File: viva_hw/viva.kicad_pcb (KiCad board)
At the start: 2 copper layers, 6 parts, among them Q1 2N3904, Q2 2N3904, Q3 2N3904, Q4 2N3904, U1 XIAO ESP32C3

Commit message: feat: updated footprints
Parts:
- removed U1: XIAO ESP32C3, RF_Module:MCU_Seeed_ESP32C3
- added J1: Conn_01x05_Socket, Connector_PinHeader_2.54mm:PinHeader_1x05_P2.54mm_Vertical, F.Cu at (164.7, 110.1)
- added M1: XIAO_ESP32C3, System_On_Chip:XIAO_ESP32C3_THR, F.Cu at (150.9, 120.4)
- moved ST7735 35.7 mm to (170.0, 111.0)

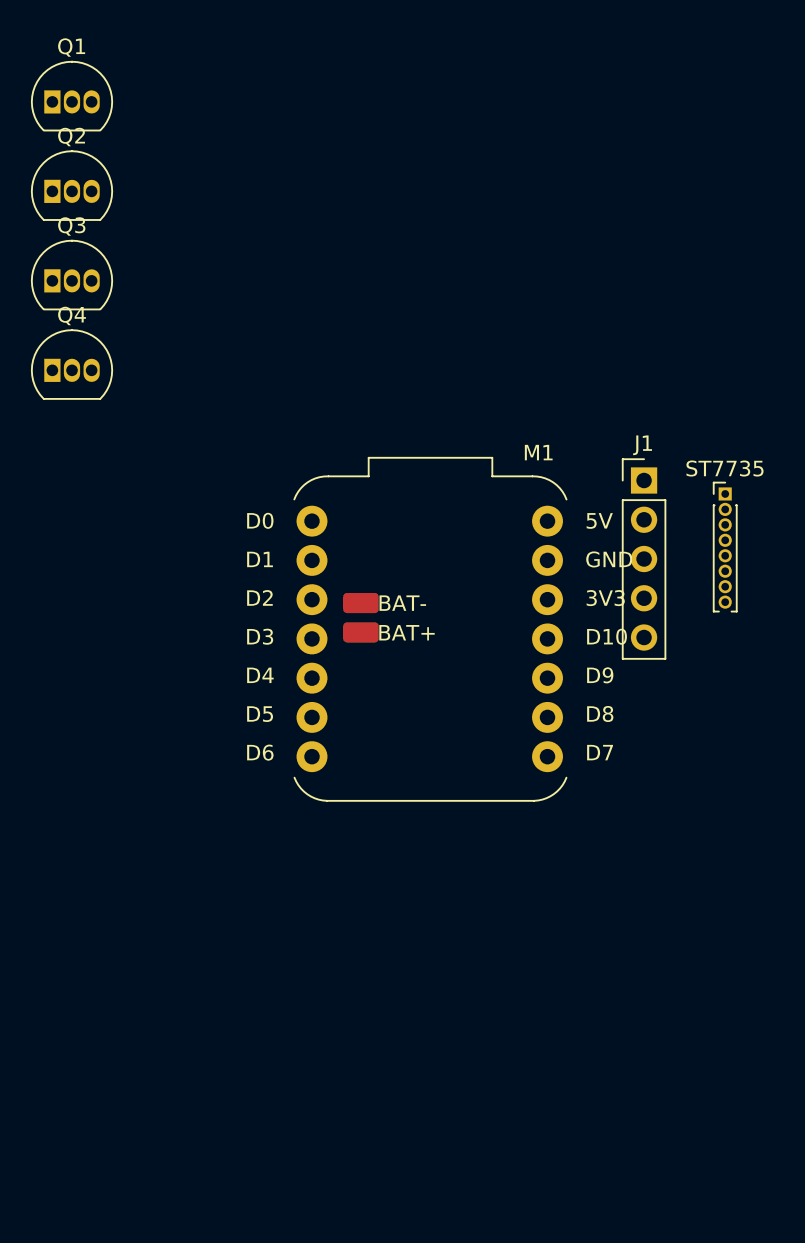
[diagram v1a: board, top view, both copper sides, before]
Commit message: feat: changed socket size for display
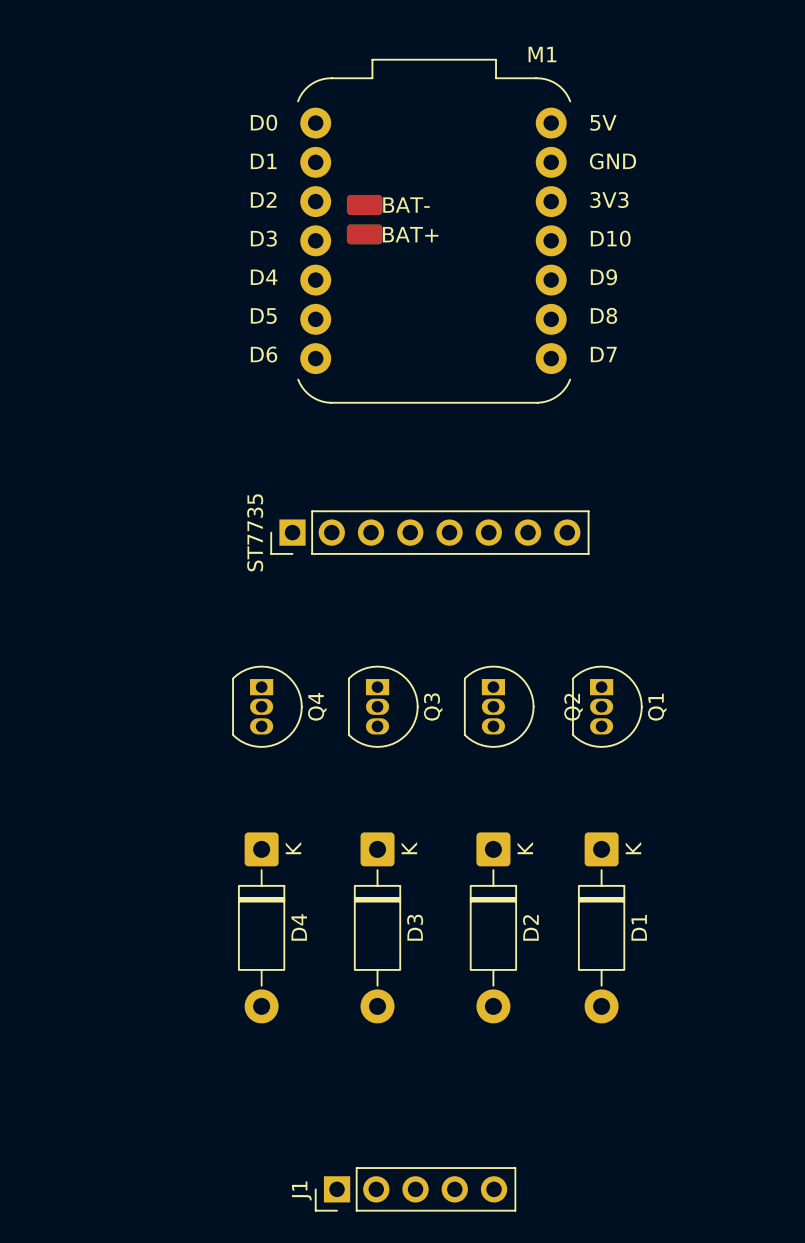
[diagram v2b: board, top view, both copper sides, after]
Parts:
- added D1: 1N4007, Diode_THT:D_DO-41_SOD81_P10.16mm_Horizontal, F.Cu at (162.0, 134.0)
- added D2: 1N4007, Diode_THT:D_DO-41_SOD81_P10.16mm_Horizontal, F.Cu at (155.0, 134.0)
- added D3: 1N4007, Diode_THT:D_DO-41_SOD81_P10.16mm_Horizontal, F.Cu at (147.5, 134.0)
- added D4: 1N4007, Diode_THT:D_DO-41_SOD81_P10.16mm_Horizontal, F.Cu at (140.0, 134.0)
- ST7735: footprint Connector_PinHeader_1.00mm:PinHeader_1x08_P1.00mm_Vertical -> Connector_PinHeader_2.54mm:PinHeader_1x08_P2.54mm_Vertical
- moved Q1 51.9 mm to (162.0, 123.5), turned to -90 degrees
- moved J1 50.0 mm to (144.9, 156.0), turned to 90 degrees
- moved Q2 42.9 mm to (155.0, 123.5), turned to -90 degrees
- moved Q3 33.7 mm to (147.5, 123.5), turned to -90 degrees
- moved ST7735 28.1 mm to (142.0, 113.5), turned to 90 degrees
- moved M1 25.8 mm to (151.2, 94.6)
- moved Q4 24.6 mm to (140.0, 123.5), turned to -90 degrees

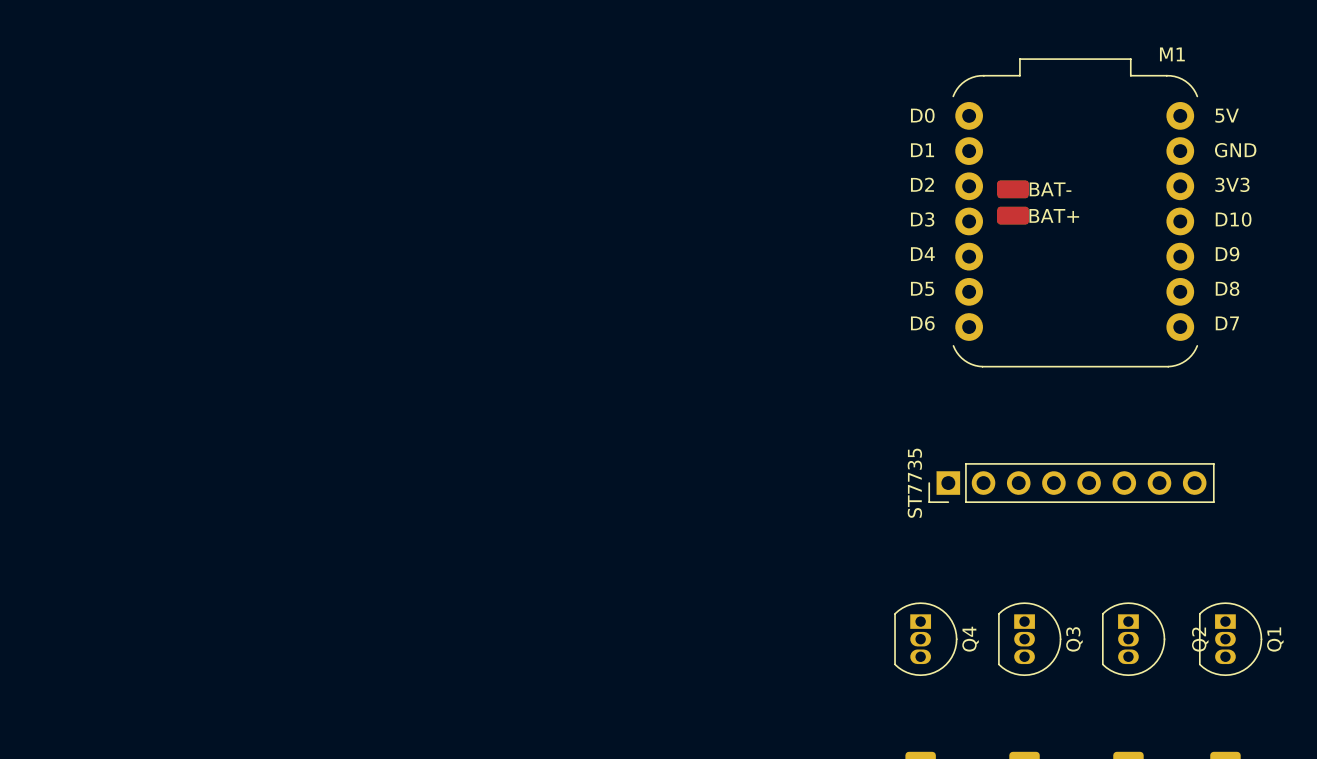
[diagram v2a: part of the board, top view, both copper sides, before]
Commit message: feat: added emg circuit
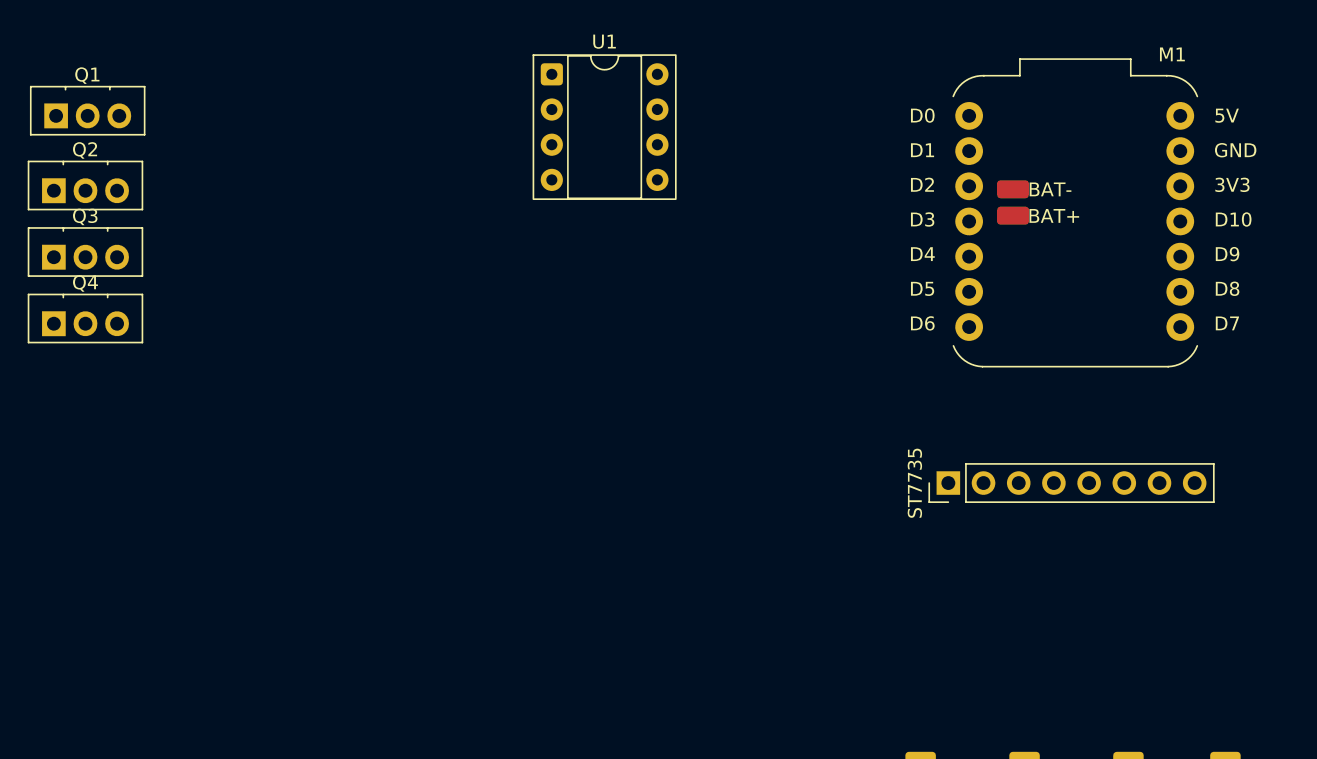
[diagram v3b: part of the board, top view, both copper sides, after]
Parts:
- added U1: LM358, Package_DIP:DIP-8_W7.62mm_Socket, F.Cu at (113.4, 84.0)
- Q1, Q2, Q3, Q4: value 2N3904 -> NMOS; footprint Package_TO_SOT_THT:TO-92_Inline -> Package_TO_SOT_THT:TO-126-3_Vertical
- moved Q1 92.0 mm to (77.6, 87.0), turned to 0 degrees
- moved Q2 83.6 mm to (77.4, 92.4), turned to 0 degrees
- moved Q3 74.8 mm to (77.4, 97.2), turned to 0 degrees
- moved Q4 66.2 mm to (77.4, 102.0), turned to 0 degrees
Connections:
- M1 pad 2: /EMG -> Net-(M1-D1)
- Q1 pad 1: 0 -> Net-(D1-A)
- Q1 pad 3: Net-(D1-A) -> 0
- Q2 pad 1: 0 -> Net-(D2-A)
- Q2 pad 3: Net-(D2-A) -> 0
- Q3 pad 1: 0 -> Net-(D3-A)
- Q3 pad 3: Net-(D3-A) -> 0
- Q4 pad 1: 0 -> Net-(D4-A)
- Q4 pad 3: Net-(D4-A) -> 0

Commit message: feat: began pcb work
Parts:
- added H1: MountingHole_Pad, MountingHole:MountingHole_2.7mm_M2.5_DIN965_Pad, F.Cu at (181.5, 40.5)
- added H2: MountingHole_Pad, MountingHole:MountingHole_2.7mm_M2.5_DIN965_Pad, F.Cu at (134.5, 40.5)
- added H3: MountingHole_Pad, MountingHole:MountingHole_2.7mm_M2.5_DIN965_Pad, F.Cu at (179.0, 100.5)
- added H4: MountingHole_Pad, MountingHole:MountingHole_2.7mm_M2.5_DIN965_Pad, F.Cu at (133.5, 101.0)
- added J2: EMG, Connector_PinHeader_2.54mm:PinHeader_1x03_P2.54mm_Vertical, F.Cu at (145.0, 100.0)
- added J3: Battery, Connector_PinHeader_2.54mm:PinHeader_1x02_P2.54mm_Vertical, F.Cu at (172.0, 66.5)
- added U2: LM358, Package_DIP:DIP-8_W7.62mm_Socket, F.Cu at (167.9, 52.0)
- J1: value Conn_01x05_Socket -> Motor
- J4: renamed from ST7735; value Conn_01x08_Socket -> ST7735
- moved Q4 91.6 mm to (163.5, 70.5), turned to 90 degrees
- moved Q3 83.0 mm to (156.0, 70.5), turned to 90 degrees
- moved Q2 73.9 mm to (148.0, 70.5), turned to 90 degrees
- moved U1 70.4 mm to (167.9, 39.5)
- moved Q1 65.5 mm to (141.0, 70.5), turned to 90 degrees
- moved D1 58.8 mm to (171.5, 76.0)
- moved D3 58.4 mm to (140.5, 76.0)
- moved J1 57.1 mm to (156.0, 100.0)
- moved D2 46.1 mm to (171.5, 91.0)
- moved M1 44.6 mm to (150.0, 50.0)
- moved D4 42.5 mm to (140.5, 91.5)
- moved J4 38.0 mm to (147.9, 76.0)
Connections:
- M1 pad 15: Net-(M1-BAT-) -> unconnected-(M1-BAT--Pad15)
- M1 pad 16: Net-(M1-BAT+) -> unconnected-(M1-BAT+-Pad16)
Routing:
- added copper zone on B.Cu, net 0

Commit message: feat: dont remember
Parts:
- removed J2: EMG, Connector_PinHeader_2.54mm:PinHeader_1x03_P2.54mm_Vertical
- removed U1, U2: LM358, Package_DIP:DIP-8_W7.62mm_Socket
- added J5: Battery, Connector_PinHeader_2.54mm:PinHeader_1x02_P2.54mm_Vertical, F.Cu at (86.0, 39.5)
- added SW4: SW_SPDT, Additional_Switches:SPDT, F.Cu at (76.7, 37.9)
- J4: value ST7735 -> OLED; footprint Connector_PinHeader_2.54mm:PinHeader_1x08_P2.54mm_Vertical -> Connector_PinHeader_2.54mm:PinHeader_1x04_P2.54mm_Vertical
- moved J4 28.5 mm to (124.0, 60.5), turned to 180 degrees
- moved H2 12.2 mm to (123.0, 36.5)
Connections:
- J3 pad 2: 0 -> Net-(J3-Pin_2)
- M1 pad 10: Net-(J4-Pin_4) -> Net-(M1-D9)
- M1 pad 11: Net-(J4-Pin_3) -> Net-(M1-D10)
- M1 pad 2: Net-(M1-D1) -> unconnected-(M1-D1-Pad2)
- M1 pad 3: Net-(J4-Pin_5) -> Net-(M1-D2)
- M1 pad 5: Net-(M1-D4) -> Net-(J4-Pin_4)
- M1 pad 6: Net-(M1-D5) -> Net-(J4-Pin_3)
- M1 pad 7: Net-(M1-D6) -> unconnected-(M1-D6-Pad7)
- M1 pad 8: Net-(J4-Pin_7) -> Net-(M1-D7)
- M1 pad 9: Net-(J4-Pin_6) -> Net-(M1-D8)
- Q1 pad 2: Net-(M1-D3) -> Net-(M1-D7)
- Q2 pad 2: Net-(M1-D4) -> Net-(M1-D8)
- Q3 pad 2: Net-(M1-D5) -> Net-(M1-D9)
- Q4 pad 2: Net-(M1-D6) -> Net-(M1-D10)

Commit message: feat: finished schematic
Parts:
- removed SW4: SW_SPDT, Additional_Switches:SPDT
- added C1: 100n, Capacitor_THT:C_Disc_D4.3mm_W1.9mm_P5.00mm, F.Cu at (160.0, 95.0)
- added C2: 100n, Capacitor_THT:C_Disc_D4.3mm_W1.9mm_P5.00mm, F.Cu at (152.0, 95.0)
- added C3: 100n, Capacitor_THT:C_Disc_D4.3mm_W1.9mm_P5.00mm, F.Cu at (144.0, 95.0)
- added C4: 100n, Capacitor_THT:C_Disc_D4.3mm_W1.9mm_P5.00mm, F.Cu at (136.0, 95.0)
- added C5: 100u, Capacitor_THT:CP_Radial_D8.0mm_P3.50mm, F.Cu at (128.5, 87.5)
- added C6: 100u, Capacitor_THT:CP_Radial_D8.0mm_P3.50mm, F.Cu at (170.0, 47.0)
- added J2: Measure_enable, Connector_PinHeader_2.54mm:PinHeader_1x02_P2.54mm_Vertical, F.Cu at (129.0, 57.5)
- added R13: 5.6k, Resistor_THT:R_Axial_DIN0207_L6.3mm_D2.5mm_P10.16mm_Horizontal, F.Cu at (125.4, 69.5)
- added R14: 5.6k, Resistor_THT:R_Axial_DIN0207_L6.3mm_D2.5mm_P10.16mm_Horizontal, F.Cu at (174.7, 69.5)
- added R3: 220k, Resistor_THT:R_Axial_DIN0207_L6.3mm_D2.5mm_P10.16mm_Horizontal, F.Cu at (132.5, 43.0)
- added R4: 220k, Resistor_THT:R_Axial_DIN0207_L6.3mm_D2.5mm_P10.16mm_Horizontal, F.Cu at (128.5, 43.0)
- added SW1: SW_DPDT_x2, Additional_Switches:SK-22D07G4, F.Cu at (172.5, 60.1)
- added SW2: SW_DPST_x2, Additional_Switches:TACTILE-2P-THT, F.Cu at (130.0, 75.5)
- added SW3: SW_DPST_x2, Additional_Switches:TACTILE-2P-THT, F.Cu at (170.0, 75.5)
- D1, D2, D3, D4: value 1N4007 -> 1N4148; footprint Diode_THT:D_DO-41_SOD81_P10.16mm_Horizontal -> Diode_THT:D_DO-34_SOD68_P7.62mm_Horizontal
- H1, H2, H3, H4: footprint MountingHole:MountingHole_2.7mm_M2.5_DIN965_Pad -> MountingHole:MountingHole_3.2mm_M3_ISO7380_Pad
- J3: value Battery -> Battery_in; footprint Connector_PinHeader_2.54mm:PinHeader_1x02_P2.54mm_Vertical -> Connector_PinHeader_2.00mm:PinHeader_1x02_P2.00mm_Vertical
- J4: footprint Connector_PinHeader_2.54mm:PinHeader_1x04_P2.54mm_Vertical -> Additional_Display:OLED_0.96
- J5: value Battery -> Battery_out; footprint Connector_PinHeader_2.54mm:PinHeader_1x02_P2.54mm_Vertical -> Connector_PinHeader_2.00mm:PinHeader_1x02_P2.00mm_Vertical
- Q1, Q2, Q3, Q4: footprint Package_TO_SOT_THT:TO-126-3_Vertical -> Package_TO_SOT_THT:TO-92L_Inline
- moved J5 81.2 mm to (166.0, 53.5)
- moved Q4 29.2 mm to (138.4, 85.5)
- moved J4 26.9 mm to (150.0, 67.5), turned to 0 degrees
- moved Q1 26.2 mm to (162.4, 85.5)
- moved D1 21.8 mm to (164.0, 96.5), turned to 90 degrees
- moved D3 21.8 mm to (148.0, 96.5), turned to 90 degrees
- moved Q3 17.8 mm to (146.4, 85.5)
- moved D2 16.4 mm to (156.1, 96.5), turned to 90 degrees
- moved Q2 16.4 mm to (154.4, 85.5)
- moved J1 11.3 mm to (144.9, 102.5)
- moved H1 10.8 mm to (171.5, 36.5)
- moved J3 8.14 mm to (166.0, 61.0)
- moved M1 7.90 mm to (149.9, 42.1)
- moved H3 7.57 mm to (171.5, 101.5)
- moved H2 5.50 mm to (128.5, 36.5)
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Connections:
- J3 pad 1: Net-(J3-Pin_1) -> 0
- J4 pad 2: /VCC -> Net-(J4-Pin_2)
- J5 pad 1: Net-(J5-Pin_1) -> 0
- J5 pad 2: Net-(J3-Pin_2) -> /VCC
- M1 pad 12: /VCC -> Net-(J4-Pin_2)
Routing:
- net /VCC: track 0.00 -> 94.1 mm
- net Net-(M1-D2): track 0.00 -> 36.9 mm
- net Net-(J4-Pin_2): track 0.00 -> 25.7 mm
- net Net-(D4-A): track 0.00 -> 25.2 mm, vias 0 -> 2
- net Net-(D1-A): track 0.00 -> 23.0 mm, vias 0 -> 2
- net Net-(D3-A): track 0.00 -> 22.8 mm, vias 0 -> 2
- net Net-(D2-A): track 0.00 -> 22.0 mm, vias 0 -> 2
- net Net-(M1-D0): track 0.00 -> 17.3 mm
- net Net-(J4-Pin_4): track 0.00 -> 16.1 mm
- net Net-(J4-Pin_3): track 0.00 -> 12.5 mm
- net Net-(M1-D3): track 0.00 -> 10.8 mm
- net Net-(J2-Pin_1): track 0.00 -> 4.55 mm
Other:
- board outline added: 53 x 75 mm

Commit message: feat: completed v_1
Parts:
- added R1: 100, Resistor_THT:R_Axial_DIN0207_L6.3mm_D2.5mm_P10.16mm_Horizontal, F.Cu at (164.8, 77.5)
- added R2: 100, Resistor_THT:R_Axial_DIN0207_L6.3mm_D2.5mm_P10.16mm_Horizontal, F.Cu at (164.8, 74.0)
- added R5: 100, Resistor_THT:R_Axial_DIN0207_L6.3mm_D2.5mm_P10.16mm_Horizontal, F.Cu at (164.8, 70.5)
- added R6: 100, Resistor_THT:R_Axial_DIN0207_L6.3mm_D2.5mm_P10.16mm_Horizontal, F.Cu at (164.8, 67.0)
- R3, R4: value 220k -> 5.6k
- moved R14 50.7 mm to (127.0, 52.2), turned to 90 degrees
- moved SW3 41.4 mm to (130.5, 63.0)
- moved R13 9.50 mm to (125.3, 79.0)
- moved C5 6.04 mm to (131.0, 93.0), turned to 180 degrees
- moved R3 3.64 mm to (136.0, 42.0)
- moved R4 3.16 mm to (131.5, 42.0)
- moved J2 3.11 mm to (131.7, 56.0)
- moved SW2 3.08 mm to (130.5, 72.5)
- moved C6 0.71 mm to (169.5, 47.5)
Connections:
- J4 pad 5: 0 -> (no net)
- J4 pad 6: 0 -> (no net)
- J4 pad 7: 0 -> (no net)
- J4 pad 8: 0 -> (no net)
- Q1 pad 2: Net-(M1-D7) -> Net-(Q1-G)
- Q2 pad 2: Net-(M1-D8) -> Net-(Q2-G)
- Q3 pad 2: Net-(M1-D9) -> Net-(Q3-G)
- Q4 pad 2: Net-(M1-D10) -> Net-(Q4-G)
- SW1 pad 7: 0 -> (no net)
- SW1 pad 8: 0 -> (no net)
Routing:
- net /VCC: track 94.1 -> 165.0 mm
- net Net-(M1-D3): track 10.8 -> 54.2 mm
- net Net-(Q4-G): track 0.00 -> 40.6 mm, vias 0 -> 1
- net Net-(M1-D10): track 0.00 -> 40.3 mm
- net Net-(Q3-G): track 0.00 -> 36.1 mm, vias 0 -> 1
- net Net-(M1-D9): track 0.00 -> 34.0 mm
- net Net-(Q2-G): track 0.00 -> 31.5 mm, vias 0 -> 1
- net Net-(M1-D8): track 0.00 -> 27.6 mm
- net Net-(Q1-G): track 0.00 -> 27.0 mm, vias 0 -> 1
- net Net-(M1-D7): track 0.00 -> 21.2 mm
- net Net-(J3-Pin_2): track 0.00 -> 19.9 mm
- net Net-(M1-D2): track 36.9 -> 44.0 mm
- net Net-(J4-Pin_2): track 25.7 -> 19.7 mm, vias 0 -> 1
- net Net-(M1-D0): track 17.3 -> 14.6 mm
- net Net-(J2-Pin_1): track 4.55 -> 3.93 mm
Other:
- outline, holes or cut-outs redrawn
- board text added: "Viva v1 06.05.2026"

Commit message: feat: v2, changed controller
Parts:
- removed C5: 100u, Capacitor_THT:CP_Radial_D8.0mm_P3.50mm
- removed J2: Measure_enable, Connector_PinHeader_2.54mm:PinHeader_1x02_P2.54mm_Vertical
- removed J5: Battery_out, Connector_PinHeader_2.00mm:PinHeader_1x02_P2.00mm_Vertical
- removed M1: XIAO_ESP32C3, System_On_Chip:XIAO_ESP32C3_THR
- removed R3, R4: 5.6k, Resistor_THT:R_Axial_DIN0207_L6.3mm_D2.5mm_P10.16mm_Horizontal
- added M2: ESP32C3_Super_Mini, System_On_Chip:ESP32C3_SUPER_MINI_THR, F.Cu at (150.0, 41.0)
- J3: value Battery_in -> Power_in; footprint Connector_PinHeader_2.00mm:PinHeader_1x02_P2.00mm_Vertical -> Additional_Connectors:Barrel_Plug_5.5mmx2.1mm
- moved C6 26.5 mm to (194.0, 57.5)
- moved J3 24.1 mm to (168.5, 37.0)
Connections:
- C1 pad 1: /VCC -> /+3V3
- C2 pad 1: /VCC -> /+3V3
- C3 pad 1: /VCC -> /+3V3
- C4 pad 1: /VCC -> /+3V3
- C6 pad 1: /VCC -> /+3V3
- D1 pad 1: /VCC -> /+3V3
- D2 pad 1: /VCC -> /+3V3
- D3 pad 1: /VCC -> /+3V3
- D4 pad 1: /VCC -> /+3V3
- J1 pad 1: /VCC -> /+3V3
- J4 pad 2: Net-(J4-Pin_2) -> /+3V3
- Q1 pad 1: Net-(D1-A) -> 0
- Q1 pad 3: 0 -> Net-(D1-A)
- Q2 pad 1: Net-(D2-A) -> 0
- Q2 pad 3: 0 -> Net-(D2-A)
- Q3 pad 1: Net-(D3-A) -> 0
- Q3 pad 3: 0 -> Net-(D3-A)
- Q4 pad 1: Net-(D4-A) -> 0
- Q4 pad 3: 0 -> Net-(D4-A)
- R13 pad 1: /VCC -> /+3V3
- R14 pad 1: /VCC -> /+3V3
- SW1 pad 3: /VCC -> /+3V3
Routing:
- net /VCC: track 165.0 -> 0.00 mm
- net Net-(M2-D2): track 54.2 -> 0.00 mm
- net Net-(M2-D1): track 44.0 -> 0.00 mm
- net Net-(Q4-G): track 40.6 -> 0.00 mm, vias 1 -> 0
- net Net-(M2-D6): track 40.3 -> 0.00 mm
- net Net-(Q3-G): track 36.1 -> 0.00 mm, vias 1 -> 0
- net Net-(M2-D7): track 34.0 -> 0.00 mm
- net Net-(Q2-G): track 31.5 -> 0.00 mm, vias 1 -> 0
- net Net-(M2-D10): track 27.6 -> 0.00 mm
- net Net-(Q1-G): track 27.0 -> 0.00 mm, vias 1 -> 0
- net Net-(D4-A): track 25.2 -> 0.00 mm, vias 2 -> 0
- net Net-(D1-A): track 23.0 -> 0.00 mm, vias 2 -> 0
- net Net-(D3-A): track 22.8 -> 0.00 mm, vias 2 -> 0
- net Net-(D2-A): track 22.0 -> 0.00 mm, vias 2 -> 0
- net Net-(M2-D3): track 21.2 -> 0.00 mm
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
